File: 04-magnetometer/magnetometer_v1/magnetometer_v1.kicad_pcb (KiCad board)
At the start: 4 copper layers, 28.5 x 23.5 mm, 42 parts, among them IC1 STM32F072CBT6, IC2 TMAG5170A1QDGKR, IC3 TCAN1042GVDRQ1, J1 Conn_02x04_Odd_Even, J2 USB4110-GF-A, SW3 SW_SPDT, U1 SPX3819M5-L-3-3/TR, U2 NANOT100AS, U3 NANOT100AS

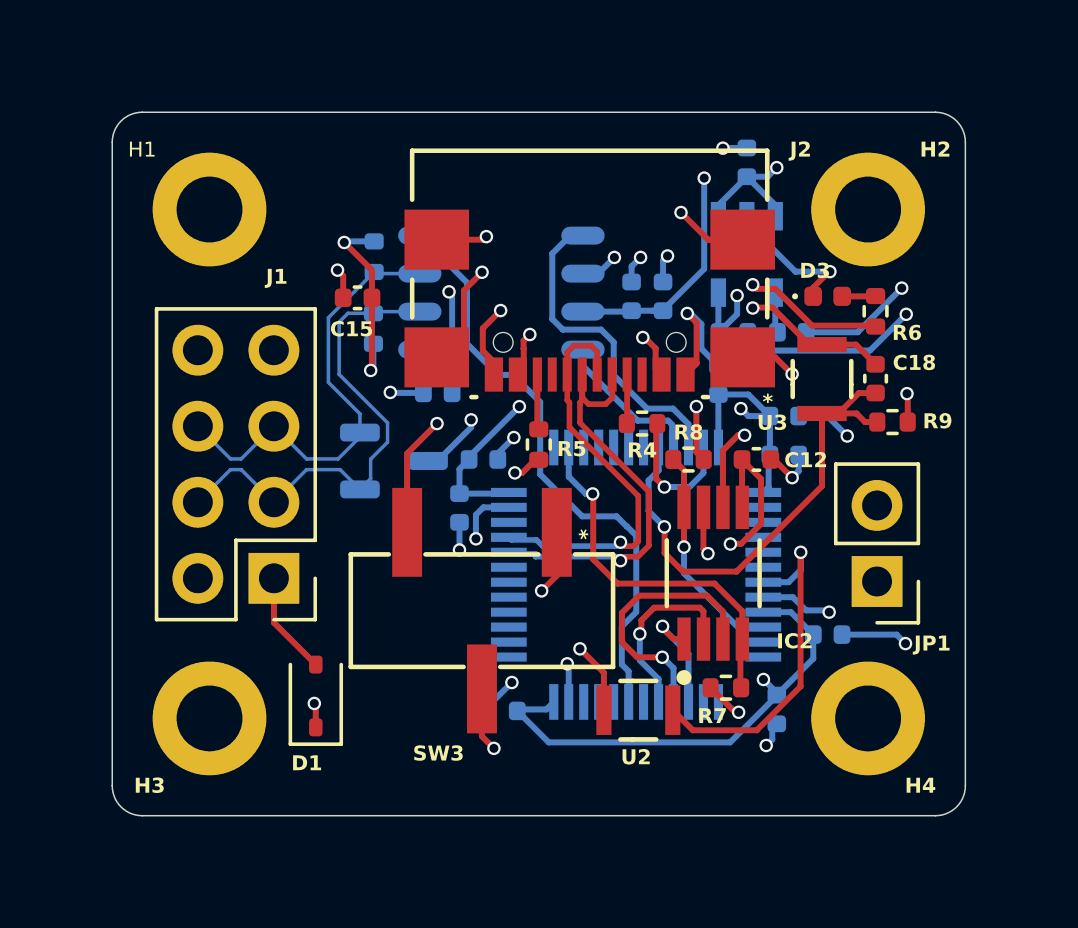
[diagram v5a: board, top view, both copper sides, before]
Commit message: fix via clearance
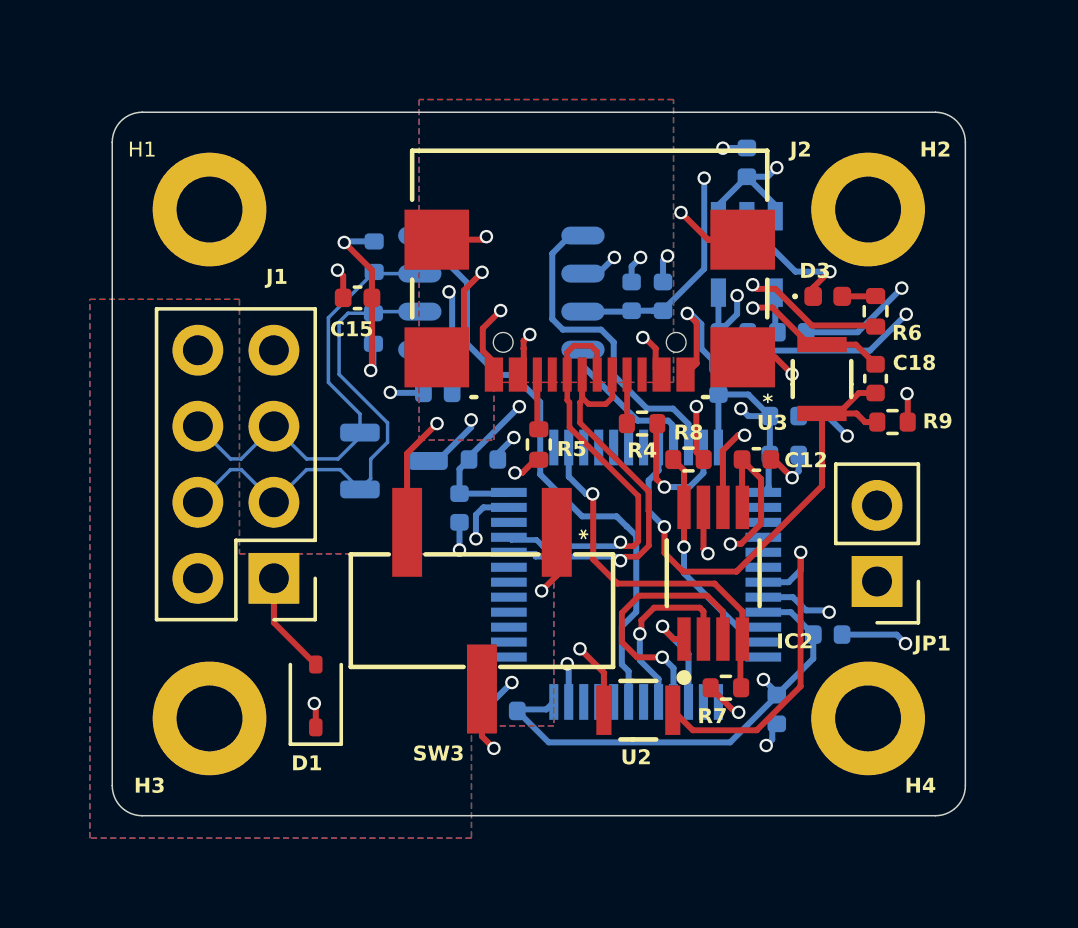
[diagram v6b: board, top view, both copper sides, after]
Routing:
- added copper zone on B.Cu, net 5v
- added copper zone on F.Cu, net 5v
- added copper zone on In1.Cu, net 5v
- added copper zone on B.Cu, net VBUS
- added copper zone on F.Cu, net VBUS
- added copper zone on In1.Cu, net VBUS
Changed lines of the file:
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@@
+	)
+	(zone
+		(net 8)
+		(net_name "5v")
+		(layers "F.Cu" "B.Cu" "In1.Cu" "In2.Cu")
+		(hatch edge 0.5)
+		(priority 1)
+		(connect_pads
+			(clearance 0.2)
+		)
+		(min_thickness 0.25)
+		(filled_areas_thickness no)
+		(fill yes
+			(thermal_gap 0.5)
+			(thermal_bridge_width 0.5)
+		)
+		(polygon
+			(pts
+				(xy 158 60) (xy 163 60) (xy 163 68.5) (xy 173.5 68.5) (xy 173.5 74.25) (xy 170.75 74.25) (xy 170.75 78)
+				(xy 158 78)
+			)
+		)
+	)
+	(zone
+		(net 52)
+		(net_name "VBUS")
+		(layers "F.Cu" "B.Cu" "In1.Cu" "In2.Cu")
+		(hatch edge 0.5)
+		(priority 3)
+		(connect_pads
+			(clearance 0.2)
+		)
+		(min_thickness 0.25)
+		(filled_areas_thickness no)
+		(fill yes
+			(thermal_gap 0.5)
+			(thermal_bridge_width 0.5)
+		)
+		(polygon
+			(pts
+				(xy 169 64.7) (xy 171.5 64.7) (xy 171.5 62.775) (xy 177.5 62.775) (xy 177.5 53.325) (xy 169 53.325)
+			)
+		)
 	)
 	(zone
@@
 		(hatch edge 0.5)
 		(connect_pads
-			(clearance 0.5)
+			(clearance 0.2)
 		)
 		(min_thickness 0.25)
@@
 		(priority 4)
 		(connect_pads
-			(clearance 0.5)
+			(clearance 0.2)
 		)
 		(min_thickness 0.25)
@@
 	)
 	(zone
-		(net 8)
-		(net_name "5v")
-		(layer "In2.Cu")
-		(hatch edge 0.5)
-		(priority 1)
-		(connect_pads
-			(clearance 0.5)
-		)
-		(min_thickness 0.25)
-		(filled_areas_thickness no)
-		(fill yes
-			(thermal_gap 0.5)
-			(thermal_bridge_width 0.5)
-		)
-		(polygon
-			(pts
-				(xy 158 60) (xy 163 60) (xy 163 68.5) (xy 173.5 68.5) (xy 173.5 74.25) (xy 170.75 74.25) (xy 170.75 78)
-				(xy 158 78)
-			)
-		)
-	)
-	(zone
 		(net 4)
 		(net_name "3v3")
@@
 		(priority 5)
 		(connect_pads
-			(clearance 0.5)
+			(clearance 0.2)
 		)
 		(min_thickness 0.25)
@@
 	)
 	(zone
-		(net 52)
-		(net_name "VBUS")
-		(layer "In2.Cu")
-		(hatch edge 0.5)
-		(priority 3)
-		(connect_pads
-			(clearance 0.5)
-		)
-		(min_thickness 0.25)
-		(filled_areas_thickness no)
-		(fill yes
-			(thermal_gap 0.5)
-			(thermal_bridge_width 0.5)
-		)
-		(polygon
-			(pts
-				(xy 169 64.7) (xy 171.5 64.7) (xy 171.5 62.775) (xy 177.5 62.775) (xy 177.5 53.325) (xy 169 53.325)
-			)
-		)
-	)
-	(zone
 		(net 55)
 		(net_name "VIN_JUMP")
@@
 		(priority 2)
 		(connect_pads
-			(clearance 0.5)
+			(clearance 0.2)
 		)
 		(min_thickness 0.25)

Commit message: fix power plane layers
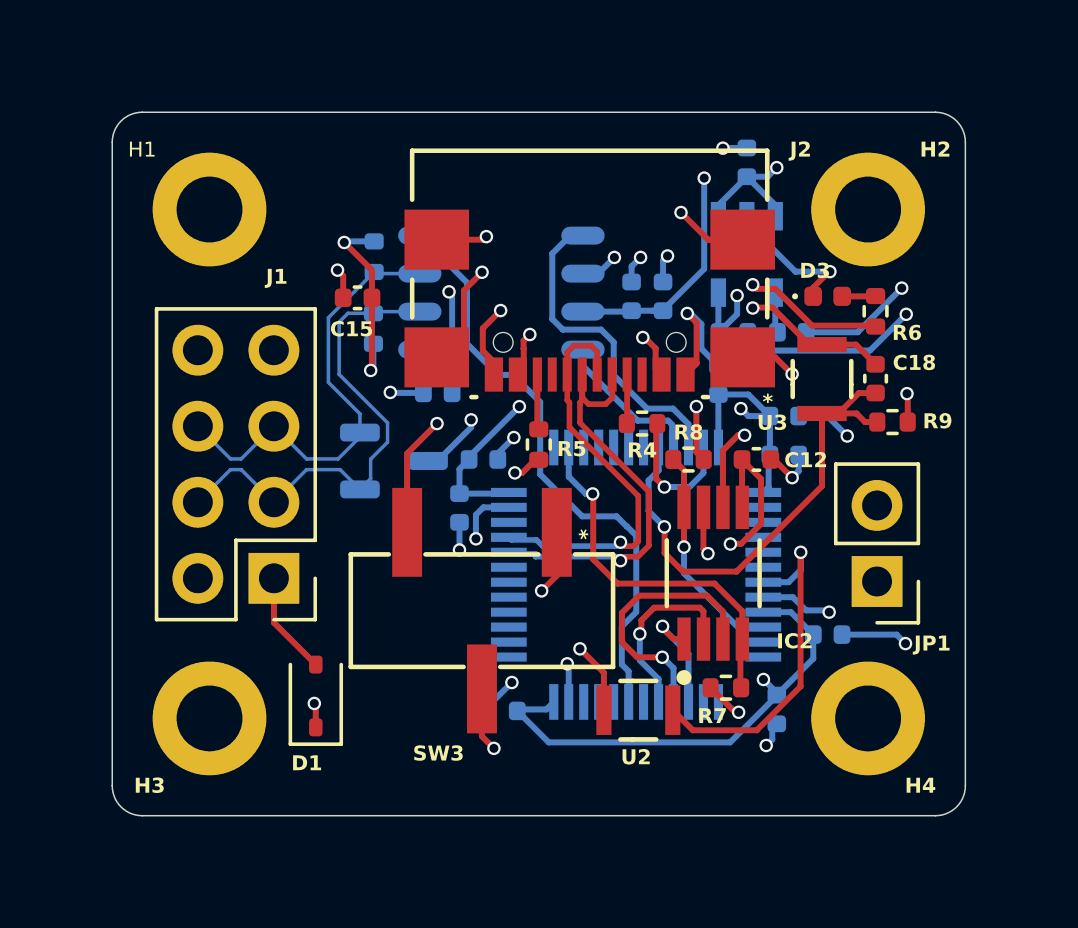
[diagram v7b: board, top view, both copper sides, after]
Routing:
- removed copper zone on B.Cu, net 5v
- removed copper zone on F.Cu, net 5v
- removed copper zone on In1.Cu, net 5v
- removed copper zone on B.Cu, net VBUS
- removed copper zone on F.Cu, net VBUS
- removed copper zone on In1.Cu, net VBUS
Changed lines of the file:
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@@
-	)
-	(zone
-		(net 8)
-		(net_name "5v")
-		(layers "F.Cu" "B.Cu" "In1.Cu" "In2.Cu")
-		(hatch edge 0.5)
-		(priority 1)
-		(connect_pads
-			(clearance 0.2)
-		)
-		(min_thickness 0.25)
-		(filled_areas_thickness no)
-		(fill yes
-			(thermal_gap 0.5)
-			(thermal_bridge_width 0.5)
-		)
-		(polygon
-			(pts
-				(xy 158 60) (xy 163 60) (xy 163 68.5) (xy 173.5 68.5) (xy 173.5 74.25) (xy 170.75 74.25) (xy 170.75 78)
-				(xy 158 78)
-			)
-		)
-	)
-	(zone
-		(net 52)
-		(net_name "VBUS")
-		(layers "F.Cu" "B.Cu" "In1.Cu" "In2.Cu")
-		(hatch edge 0.5)
-		(priority 3)
-		(connect_pads
-			(clearance 0.2)
-		)
-		(min_thickness 0.25)
-		(filled_areas_thickness no)
-		(fill yes
-			(thermal_gap 0.5)
-			(thermal_bridge_width 0.5)
-		)
-		(polygon
-			(pts
-				(xy 169 64.7) (xy 171.5 64.7) (xy 171.5 62.775) (xy 177.5 62.775) (xy 177.5 53.325) (xy 169 53.325)
-			)
-		)
 	)
 	(zone
@@
 	)
 	(zone
+		(net 8)
+		(net_name "5v")
+		(layer "In2.Cu")
+		(hatch edge 0.5)
+		(priority 1)
+		(connect_pads
+			(clearance 0.2)
+		)
+		(min_thickness 0.25)
+		(filled_areas_thickness no)
+		(fill yes
+			(thermal_gap 0.5)
+			(thermal_bridge_width 0.5)
+		)
+		(polygon
+			(pts
+				(xy 158 60) (xy 163 60) (xy 163 68.5) (xy 173.5 68.5) (xy 173.5 74.25) (xy 170.75 74.25) (xy 170.75 78)
+				(xy 158 78)
+			)
+		)
+	)
+	(zone
 		(net 4)
 		(net_name "3v3")
@@
 			)
 		)
+	)
+	(zone
+		(net 52)
+		(net_name "VBUS")
+		(layer "In2.Cu")
+		(hatch edge 0.5)
+		(priority 3)
+		(connect_pads
+			(clearance 0.2)
+		)
+		(min_thickness 0.25)
+		(filled_areas_thickness no)
+		(fill yes
+			(thermal_gap 0.5)
+			(thermal_bridge_width 0.5)
+		)
+		(polygon
+			(pts
+				(xy 169 64.7) (xy 171.5 64.7) (xy 171.5 62.775) (xy 177.5 62.775) (xy 177.5 53.325) (xy 169 53.325)
+			)
+		)

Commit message: fix filled zones
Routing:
- added copper zone on B.Cu, net (none)
- added copper zone on F.Cu, net (none)
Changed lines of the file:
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@@
+	)
+	(zone
+		(net 0)
+		(net_name "")
+		(layer "F.Cu")
+		(hatch edge 0.5)
+		(priority 6)
+		(connect_pads
+			(clearance 0.2)
+		)
+		(min_thickness 0.25)
+		(filled_areas_thickness no)
+		(fill yes
+			(thermal_gap 0.5)
+			(thermal_bridge_width 0.5)
+			(island_removal_mode 1)
+			(island_area_min 10)
+		)
+		(polygon
+			(pts
+				(xy 157 52) (xy 189 52) (xy 189 79) (xy 157 79)
+			)
+		)
+	)
+	(zone
+		(net 0)
+		(net_name "")
+		(layer "B.Cu")
+		(hatch edge 0.5)
+		(priority 7)
+		(connect_pads
+			(clearance 0.2)
+		)
+		(min_thickness 0.25)
+		(filled_areas_thickness no)
+		(fill yes
+			(thermal_gap 0.5)
+			(thermal_bridge_width 0.5)
+			(island_removal_mode 1)
+			(island_area_min 10)
+		)
+		(polygon
+			(pts
+				(xy 158 53) (xy 189 53) (xy 189 79) (xy 158 79)
+			)
+		)
 	)
 	(zone
